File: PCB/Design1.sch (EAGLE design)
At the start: 39 parts, among them J1 FTDI_DEVICE, U1 ATMEGA2560AU, Y1 16MHZ

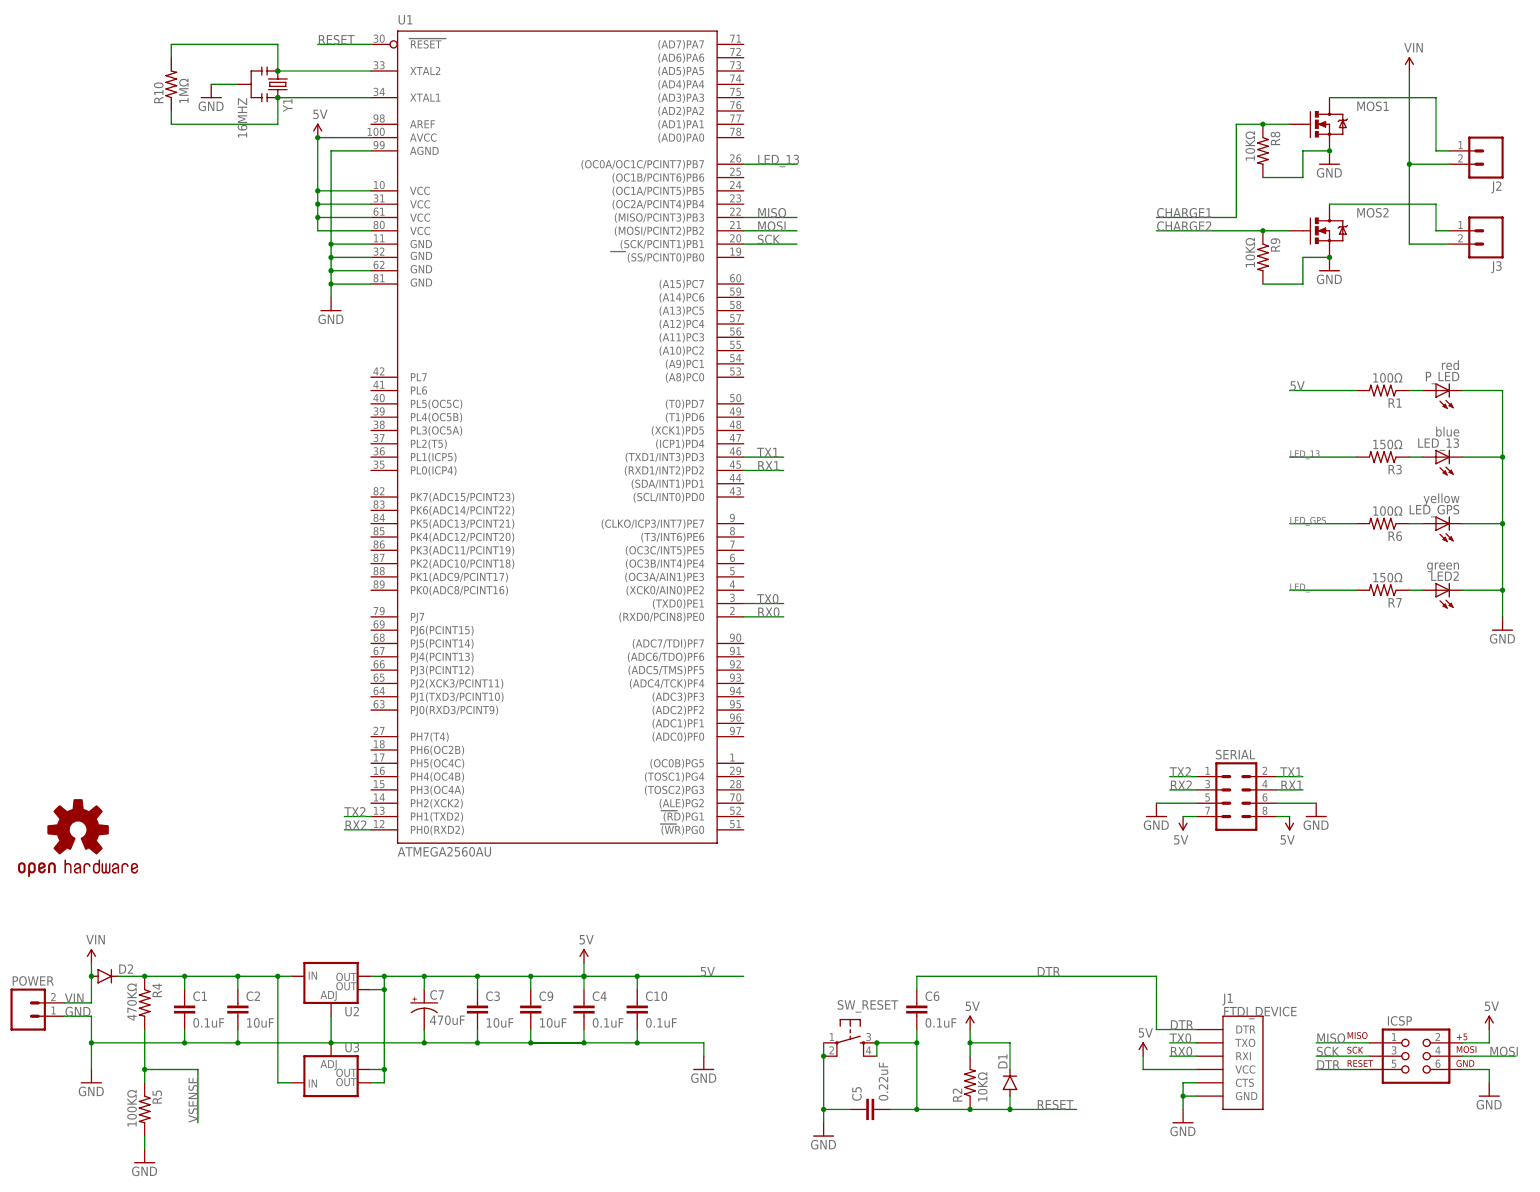
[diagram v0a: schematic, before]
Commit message: Finalize part locations; Route most of the traces 2
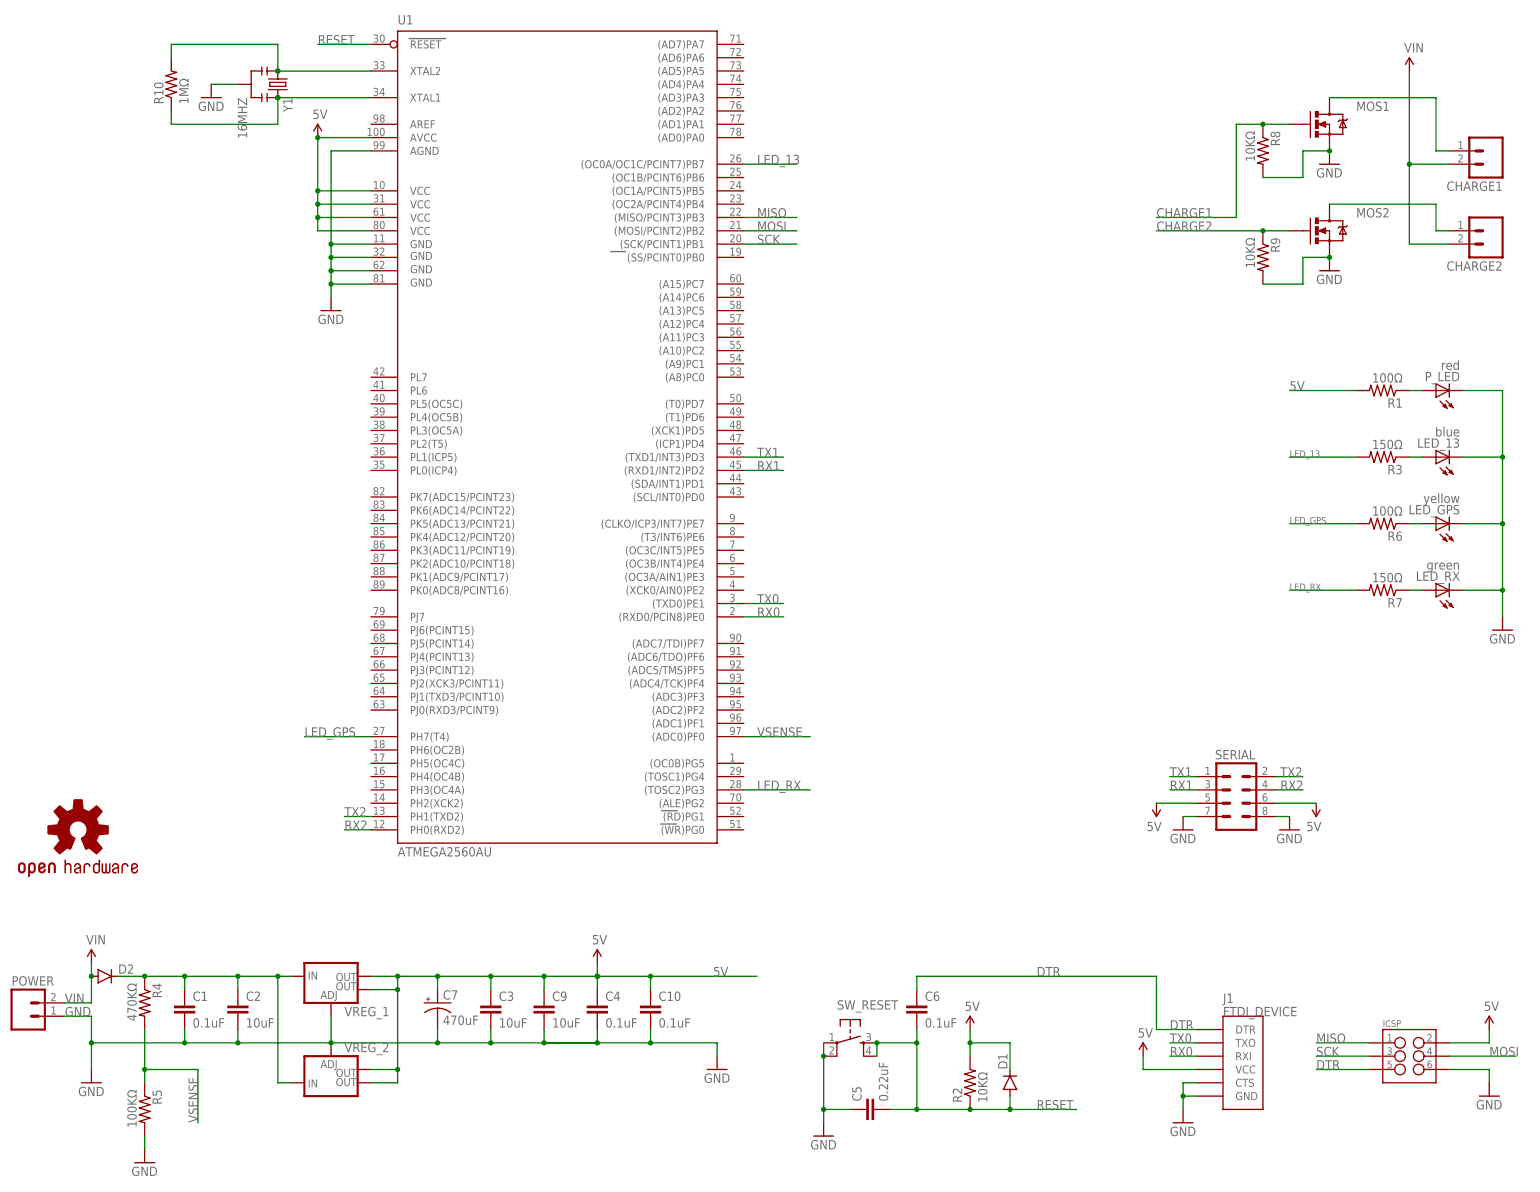
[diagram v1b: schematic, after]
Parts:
- ICSP: value AVR_SPI_PRG_6PTH -> (none); device SparkFun-Connectors:AVR_SPI_PRG_6PTH -> SparkFun-Connectors:M03X2FEMALE_SMD
- POWER: device SparkFun-Connectors:M02LOCK -> SparkFun-Connectors:M02LOCK_LONGPADS
- renumbered J2 to CHARGE1, J3 to CHARGE2, LED2 to LED_RX, U2 to VREG_1, U3 to VREG_2
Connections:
- removed net LED_: R7.2
- new net LED_RX: R7.2, U1.(TOSC2)PG3
- net 5V: now also SERIAL.5, SERIAL.6; no longer SERIAL.7, SERIAL.8
- net GND: now also SERIAL.7, SERIAL.8; no longer SERIAL.5, SERIAL.6
- net LED_GPS: now also U1.PH7(T4)
- net RX1: now also SERIAL.3; no longer SERIAL.4
- net RX2: now also SERIAL.4; no longer SERIAL.3
- net TX1: now also SERIAL.1; no longer SERIAL.2
- net TX2: now also SERIAL.2; no longer SERIAL.1
- net VSENSE: now also U1.(ADC0)PF0
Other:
- moved on the sheet: C10, C3, C4, C7, C9

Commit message: Finish routing.  Minor changes 2
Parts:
- added I2C: (no value), SparkFun-Connectors:M03X2FEMALE_SMD
- added TX/RX: (no value), SparkFun-Connectors:M06SILK_FEMALE_PTH
- 13: value blue -> (none)
- GPS: value yellow -> (none)
- J1: value FTDI_DEVICE -> FTDI
- RX: value green -> (none)
- renumbered LED_13 to 13, LED_GPS to GPS, LED_RX to RX
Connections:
- new net ADC14: I2C.4, U1.PK6(ADC14/PCINT22)
- new net ADC15: I2C.6, U1.PK7(ADC15/PCINT23)
- new net SCL: I2C.1, U1.(SCL/INT0)PD0
- new net SDA: I2C.2, U1.(SDA/INT1)PD1
- net 5V: now also I2C.5
- net GND: now also I2C.3
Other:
- note added: "Clock"
- note added: "blue"
- note added: "green"
- note added: "red"
- note added: "yellow"
- moved on the sheet: ICSP, R10, U1, Y1

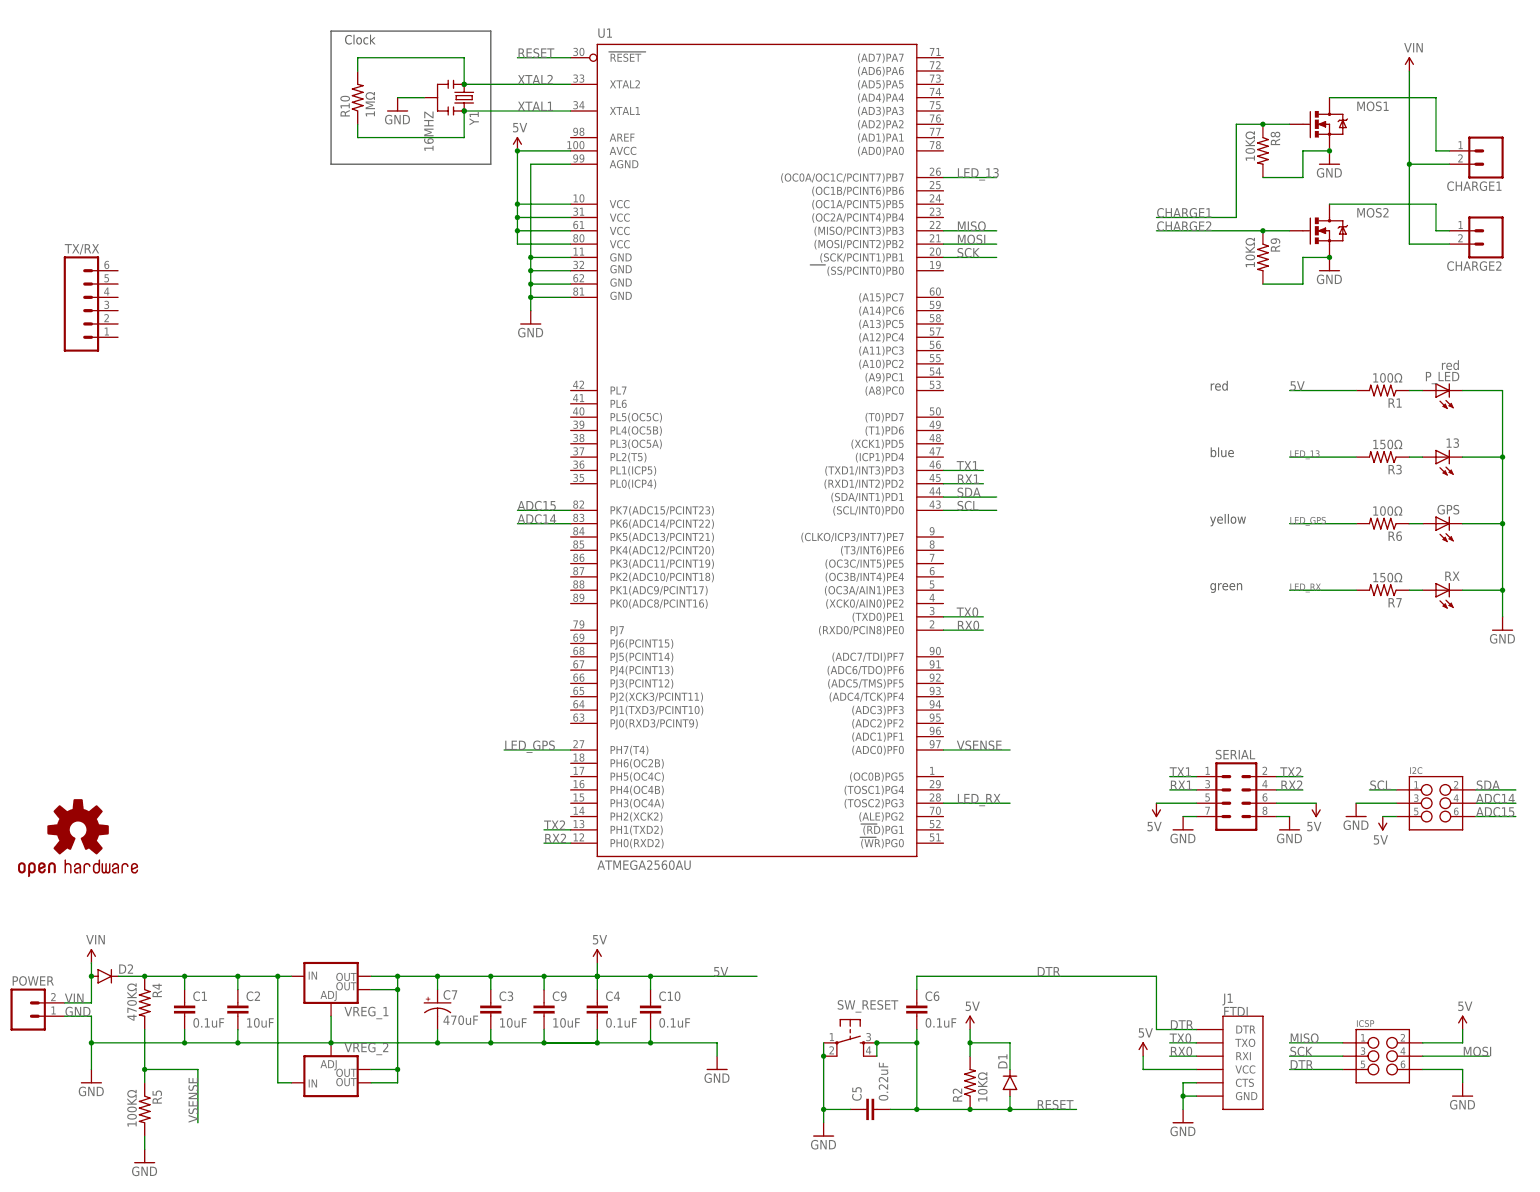
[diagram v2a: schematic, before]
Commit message: Removed 1x 5v regulator; relabeling
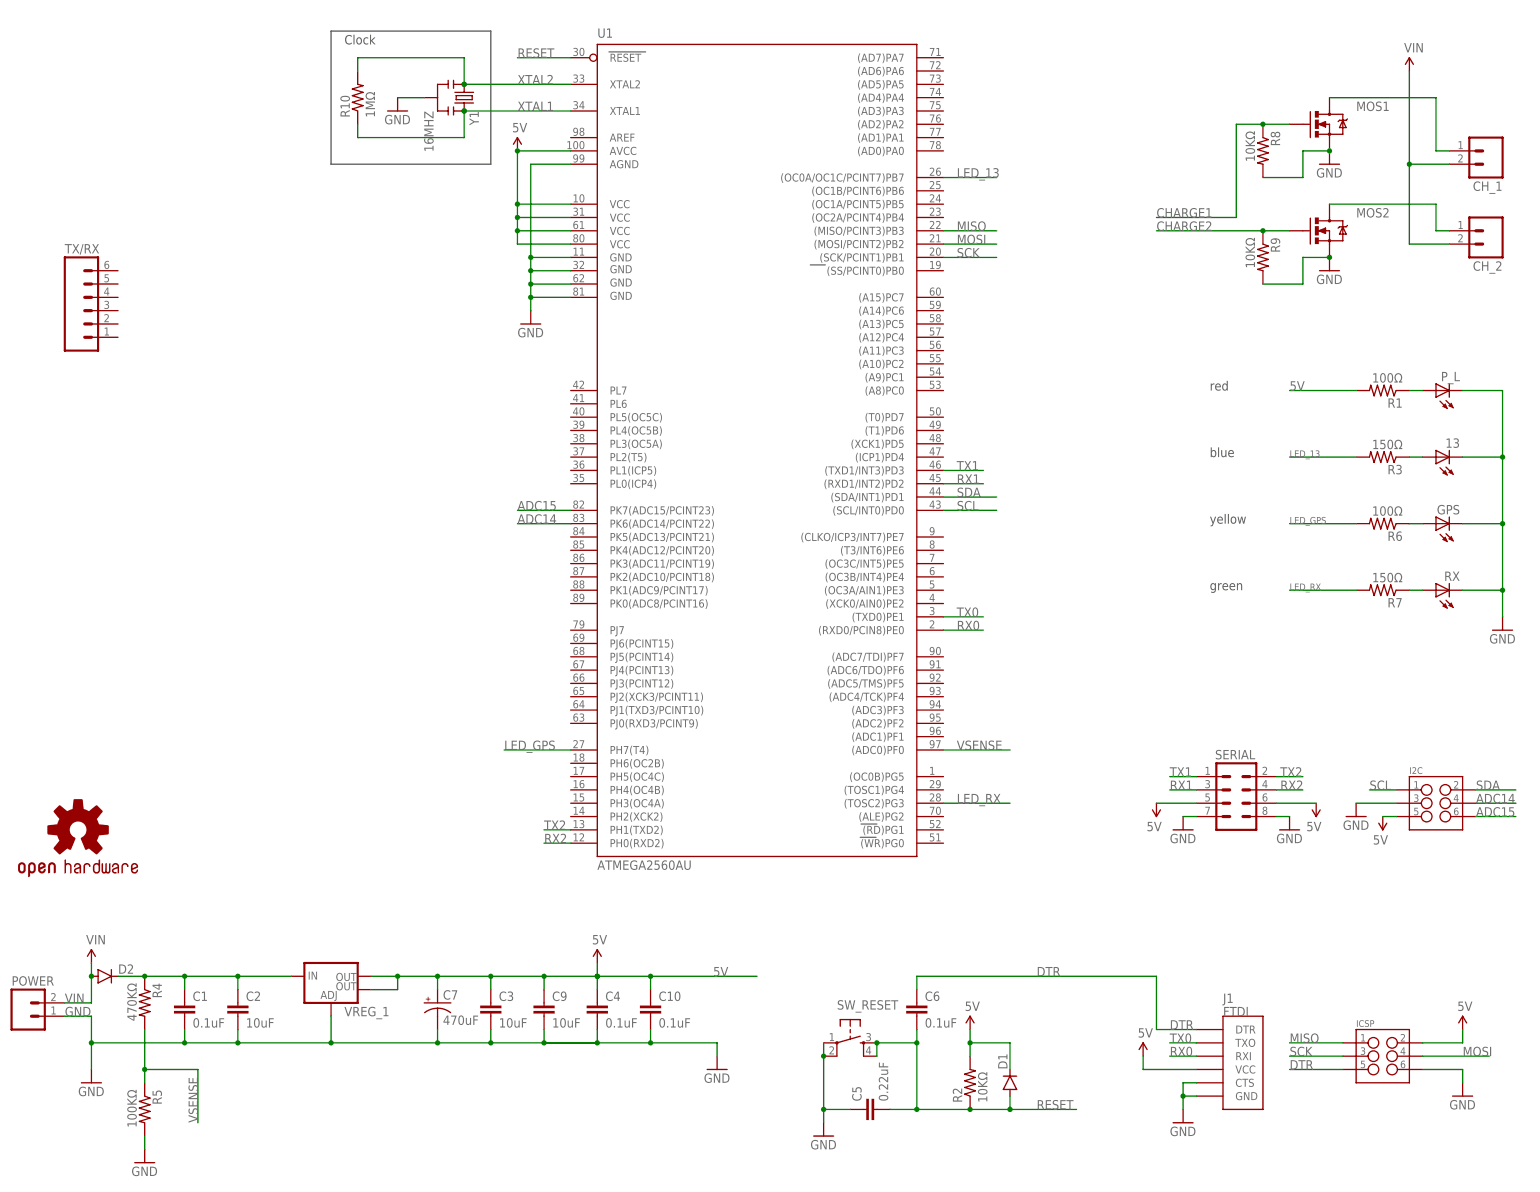
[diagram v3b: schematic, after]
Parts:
- removed VREG_2: (no value), SparkFun-PowerIC:V_REG_LM1117SOT223
- P_L: value red -> (none)
- renumbered CHARGE1 to CH_1, CHARGE2 to CH_2, P_LED to P_L
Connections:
- net 5V: no longer VREG_2.OUT, VREG_2.OUT@1
- net GND: no longer VREG_2.ADJ
- net VIN_RECTIFIED: no longer VREG_2.IN
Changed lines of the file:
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@@
 <part name="SUPPLY2" library="SparkFun-Aesthetics" deviceset="5V" device=""/>
 <part name="GND13" library="SparkFun-Aesthetics" deviceset="GND" device=""/>
-<part name="P_LED" library="led" deviceset="LED" device="SML0805" value="red"/>
+<part name="P_L" library="led" deviceset="LED" device="SML0805"/>
 <part name="R1" library="SparkFun-Resistors" deviceset="RESISTOR" device="1206" value="100Ω"/>
 <part name="GPS" library="led" deviceset="LED" device="SML0805"/>
@@
 <part name="SUPPLY8" library="SparkFun-Aesthetics" deviceset="VIN" device=""/>
 <part name="SUPPLY9" library="SparkFun-Aesthetics" deviceset="VIN" device=""/>
-<part name="CHARGE1" library="SparkFun-Connectors" deviceset="M02" device="LOCK_LONGPADS"/>
-<part name="CHARGE2" library="SparkFun-Connectors" deviceset="M02" device="LOCK_LONGPADS"/>
+<part name="CH_1" library="SparkFun-Connectors" deviceset="M02" device="LOCK_LONGPADS"/>
+<part name="CH_2" library="SparkFun-Connectors" deviceset="M02" device="LOCK_LONGPADS"/>
 <part name="VREG_1" library="SparkFun-PowerIC" deviceset="V_REG_LM1117" device="SOT223"/>
-<part name="VREG_2" library="SparkFun-PowerIC" deviceset="V_REG_LM1117" device="SOT223"/>
 <part name="C7" library="SparkFun-Capacitors" deviceset="CAP_POL" device="PTH1" value="470uF"/>
 <part name="Y1" library="SparkFun-FreqCtrl" deviceset="RESONATOR" device="16MHZ" value="16MHZ"/>
@@
 <instance part="SUPPLY2" gate="G$1" x="279.4" y="30.48"/>
 <instance part="GND13" gate="1" x="287.02" y="106.68"/>
-<instance part="P_LED" gate="G$1" x="274.32" y="152.4" rot="R90"/>
+<instance part="P_L" gate="G$1" x="274.32" y="152.4" rot="R90"/>
 <instance part="R1" gate="G$1" x="264.16" y="152.4" rot="R180"/>
 <instance part="GPS" gate="G$1" x="274.32" y="127" rot="R90"/>
@@
 <instance part="SUPPLY8" gate="G$1" x="269.24" y="213.36"/>
 <instance part="SUPPLY9" gate="G$1" x="17.78" y="43.18"/>
-<instance part="CHARGE1" gate="G$1" x="284.48" y="198.12" rot="R180"/>
-<instance part="CHARGE2" gate="G$1" x="284.48" y="182.88" rot="R180"/>
+<instance part="CH_1" gate="G$1" x="284.48" y="198.12" rot="R180"/>
+<instance part="CH_2" gate="G$1" x="284.48" y="182.88" rot="R180"/>
 <instance part="VREG_1" gate="G$1" x="63.5" y="40.64"/>
-<instance part="VREG_2" gate="G$1" x="63.5" y="20.32" rot="MR180"/>
 <instance part="C7" gate="G$1" x="83.82" y="35.56"/>
 <instance part="Y1" gate="G$1" x="88.9" y="208.28" rot="R270"/>
@@
 <pinref part="13" gate="G$1" pin="C"/>
 <wire x1="287.02" y1="139.7" x2="279.4" y2="139.7" width="0.1524" layer="91"/>
-<pinref part="P_LED" gate="G$1" pin="C"/>
+<pinref part="P_L" gate="G$1" pin="C"/>
 <pinref part="GND13" gate="1" pin="GND"/>
 <wire x1="287.02" y1="109.22" x2="287.02" y2="114.3" width="0.1524" layer="91"/>
@@
 <label x="12.7" y="33.02" size="1.778" layer="95"/>
 <junction x="45.72" y="27.94"/>
-<pinref part="VREG_2" gate="G$1" pin="ADJ"/>
 <wire x1="45.72" y1="27.94" x2="63.5" y2="27.94" width="0.1524" layer="91"/>
 <pinref part="GND9" gate="1" pin="GND"/>
@@
 <wire x1="76.2" y1="38.1" x2="76.2" y2="40.64" width="0.1524" layer="91"/>
 <junction x="76.2" y="40.64"/>
-<pinref part="VREG_2" gate="G$1" pin="OUT"/>
-<wire x1="71.12" y1="20.32" x2="76.2" y2="20.32" width="0.1524" layer="91"/>
-<wire x1="76.2" y1="20.32" x2="76.2" y2="22.86" width="0.1524" layer="91"/>
-<pinref part="VREG_2" gate="G$1" pin="OUT@1"/>
-<wire x1="76.2" y1="22.86" x2="71.12" y2="22.86" width="0.1524" layer="91"/>
-<wire x1="76.2" y1="22.86" x2="76.2" y2="38.1" width="0.1524" layer="91"/>
-<junction x="76.2" y="22.86"/>
-<junction x="76.2" y="38.1"/>
 <pinref part="C7" gate="G$1" pin="+"/>
 <wire x1="83.82" y1="40.64" x2="83.82" y2="38.1" width="0.1524" layer="91"/>
@@
 <wire x1="269.24" y1="213.36" x2="269.24" y2="195.58" width="0.1524" layer="91"/>
 <wire x1="269.24" y1="195.58" x2="269.24" y2="180.34" width="0.1524" layer="91"/>
-<pinref part="CHARGE2" gate="G$1" pin="2"/>
+<pinref part="CH_2" gate="G$1" pin="2"/>
 <wire x1="276.86" y1="180.34" x2="269.24" y2="180.34" width="0.1524" layer="91"/>
-<pinref part="CHARGE1" gate="G$1" pin="2"/>
+<pinref part="CH_1" gate="G$1" pin="2"/>
 <wire x1="276.86" y1="195.58" x2="269.24" y2="195.58" width="0.1524" layer="91"/>
 <junction x="269.24" y="195.58"/>
@@
 <net name="N$2" class="0">
 <segment>
-<pinref part="P_LED" gate="G$1" pin="A"/>
+<pinref part="P_L" gate="G$1" pin="A"/>
 <wire x1="269.24" y1="152.4" x2="271.78" y2="152.4" width="0.1524" layer="91"/>
 <pinref part="R1" gate="G$1" pin="1"/>
@@
 <wire x1="254" y1="208.28" x2="274.32" y2="208.28" width="0.1524" layer="91"/>
 <wire x1="274.32" y1="208.28" x2="274.32" y2="198.12" width="0.1524" layer="91"/>
-<pinref part="CHARGE1" gate="G$1" pin="1"/>
+<pinref part="CH_1" gate="G$1" pin="1"/>
 <wire x1="274.32" y1="198.12" x2="276.86" y2="198.12" width="0.1524" layer="91"/>
 </segment>
@@
 <segment>
 <pinref part="MOS2" gate="G$1" pin="D"/>
-<pinref part="CHARGE2" gate="G$1" pin="1"/>
+<pinref part="CH_2" gate="G$1" pin="1"/>
 <wire x1="274.32" y1="187.96" x2="274.32" y2="182.88" width="0.1524" layer="91"/>
 <wire x1="274.32" y1="182.88" x2="276.86" y2="182.88" width="0.1524" layer="91"/>
@@
 <pinref part="C2" gate="G$1" pin="1"/>
 <wire x1="35.56" y1="40.64" x2="45.72" y2="40.64" width="0.1524" layer="91"/>
-<wire x1="45.72" y1="40.64" x2="53.34" y2="40.64" width="0.1524" layer="91"/>
-<wire x1="53.34" y1="40.64" x2="55.88" y2="40.64" width="0.1524" layer="91"/>
+<wire x1="45.72" y1="40.64" x2="55.88" y2="40.64" width="0.1524" layer="91"/>
 <wire x1="45.72" y1="38.1" x2="45.72" y2="40.64" width="0.1524" layer="91"/>
 <junction x="45.72" y="40.64"/>
@@
 <junction x="35.56" y="40.64"/>
 <pinref part="VREG_1" gate="G$1" pin="IN"/>
-<wire x1="53.34" y1="40.64" x2="53.34" y2="20.32" width="0.1524" layer="91"/>
-<junction x="53.34" y="40.64"/>
-<pinref part="VREG_2" gate="G$1" pin="IN"/>
-<wire x1="53.34" y1="20.32" x2="55.88" y2="20.32" width="0.1524" layer="91"/>
-</segment>
-</net>
+</segment>
+</net>
